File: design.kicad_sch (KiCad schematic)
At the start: 11 parts, among them J1 Conn_01x03_Female

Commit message: scramble
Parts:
- J1: footprint Connector_PinHeader_2.54mm:PinHeader_1x03_P2.54mm_Horizontal -> Connector_PinHeader_2.54mm:PinHeader_1x03_P2.54mm_Vertical
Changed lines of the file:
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@@
     (property "Reference" "J1" (id 0) (at 70.485 77.47 0))
     (property "Value" "Conn_01x03_Female" (id 1) (at 70.485 80.01 0))
-    (property "Footprint" "Connector_PinHeader_2.54mm:PinHeader_1x03_P2.54mm_Horizontal" (id 2) (at 69.85 85.09 0)
+    (property "Footprint" "Connector_PinHeader_2.54mm:PinHeader_1x03_P2.54mm_Vertical" (id 2) (at 69.85 85.09 0)
       (effects (font (size 1.27 1.27)) hide)
     )
@@
     )
     (path "/59340309-930f-44a7-9dc0-119af0640901"
-      (reference "J1") (unit 1) (value "Conn_01x03_Female") (footprint "Connector_PinHeader_2.54mm:PinHeader_1x03_P2.54mm_Horizontal")
+      (reference "J1") (unit 1) (value "Conn_01x03_Female") (footprint "Connector_PinHeader_2.54mm:PinHeader_1x03_P2.54mm_Vertical")
     )
     (path "/befcbf5f-cf66-4a10-8c7a-e7785ca8eeda"

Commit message: changed to custom sk6805 footprint
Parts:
- D1, D2, D3, D4, D5, D6, D7, D8, D9: footprint LED_SMD:LED_SK6812_EC15_1.5x1.5mm -> LED_custom:LED_SK6805_EC15_1.5x1.5mm
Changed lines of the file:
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@@
     (property "Reference" "D4" (id 0) (at 115.57 114.4143 0))
     (property "Value" "SK6805_1515" (id 1) (at 115.57 116.9543 0))
-    (property "Footprint" "LED_SMD:LED_SK6812_EC15_1.5x1.5mm" (id 2) (at 104.14 126.365 0)
+    (property "Footprint" "LED_custom:LED_SK6805_EC15_1.5x1.5mm" (id 2) (at 104.14 126.365 0)
       (effects (font (size 1.27 1.27)) (justify left top) hide)
     )
@@
     (property "Reference" "D2" (id 0) (at 149.225 80.7593 0))
     (property "Value" "SK6805_1515" (id 1) (at 149.225 83.2993 0))
-    (property "Footprint" "LED_SMD:LED_SK6812_EC15_1.5x1.5mm" (id 2) (at 137.795 92.71 0)
+    (property "Footprint" "LED_custom:LED_SK6805_EC15_1.5x1.5mm" (id 2) (at 137.795 92.71 0)
       (effects (font (size 1.27 1.27)) (justify left top) hide)
     )
@@
     (property "Reference" "D8" (id 0) (at 149.225 146.1643 0))
     (property "Value" "SK6805_1515" (id 1) (at 149.225 148.7043 0))
-    (property "Footprint" "LED_SMD:LED_SK6812_EC15_1.5x1.5mm" (id 2) (at 137.795 158.115 0)
+    (property "Footprint" "LED_custom:LED_SK6805_EC15_1.5x1.5mm" (id 2) (at 137.795 158.115 0)
       (effects (font (size 1.27 1.27)) (justify left top) hide)
     )
@@
     (property "Reference" "D6" (id 0) (at 181.61 114.4143 0))
     (property "Value" "SK6805_1515" (id 1) (at 181.61 116.9543 0))
-    (property "Footprint" "LED_SMD:LED_SK6812_EC15_1.5x1.5mm" (id 2) (at 170.18 126.365 0)
+    (property "Footprint" "LED_custom:LED_SK6805_EC15_1.5x1.5mm" (id 2) (at 170.18 126.365 0)
       (effects (font (size 1.27 1.27)) (justify left top) hide)
     )
@@
     (property "Reference" "D3" (id 0) (at 181.61 80.7593 0))
     (property "Value" "SK6805_1515" (id 1) (at 181.61 83.2993 0))
-    (property "Footprint" "LED_SMD:LED_SK6812_EC15_1.5x1.5mm" (id 2) (at 170.18 92.71 0)
+    (property "Footprint" "LED_custom:LED_SK6805_EC15_1.5x1.5mm" (id 2) (at 170.18 92.71 0)
       (effects (font (size 1.27 1.27)) (justify left top) hide)
     )
@@
     (property "Reference" "D7" (id 0) (at 115.57 146.1643 0))
     (property "Value" "SK6805_1515" (id 1) (at 115.57 148.7043 0))
-    (property "Footprint" "LED_SMD:LED_SK6812_EC15_1.5x1.5mm" (id 2) (at 104.14 158.115 0)
+    (property "Footprint" "LED_custom:LED_SK6805_EC15_1.5x1.5mm" (id 2) (at 104.14 158.115 0)
       (effects (font (size 1.27 1.27)) (justify left top) hide)
     )
@@
     (property "Reference" "D1" (id 0) (at 115.57 80.7593 0))
     (property "Value" "SK6805_1515" (id 1) (at 115.57 83.2993 0))
-    (property "Footprint" "LED_SMD:LED_SK6812_EC15_1.5x1.5mm" (id 2) (at 104.14 92.71 0)
+    (property "Footprint" "LED_custom:LED_SK6805_EC15_1.5x1.5mm" (id 2) (at 104.14 92.71 0)
       (effects (font (size 1.27 1.27)) (justify left top) hide)
     )
@@
     (property "Reference" "D5" (id 0) (at 149.225 114.4143 0))
     (property "Value" "SK6805_1515" (id 1) (at 149.225 116.9543 0))
-    (property "Footprint" "LED_SMD:LED_SK6812_EC15_1.5x1.5mm" (id 2) (at 137.795 126.365 0)
+    (property "Footprint" "LED_custom:LED_SK6805_EC15_1.5x1.5mm" (id 2) (at 137.795 126.365 0)
       (effects (font (size 1.27 1.27)) (justify left top) hide)
     )
@@
     (property "Reference" "D9" (id 0) (at 181.61 146.1643 0))
     (property "Value" "SK6805_1515" (id 1) (at 181.61 148.7043 0))
-    (property "Footprint" "LED_SMD:LED_SK6812_EC15_1.5x1.5mm" (id 2) (at 170.18 158.115 0)
+    (property "Footprint" "LED_custom:LED_SK6805_EC15_1.5x1.5mm" (id 2) (at 170.18 158.115 0)
       (effects (font (size 1.27 1.27)) (justify left top) hide)
     )
@@
     )
     (path "/e522fa02-5074-425d-83fb-e4bbcbcfc1cc"
-      (reference "D1") (unit 1) (value "SK6805_1515") (footprint "LED_SMD:LED_SK6812_EC15_1.5x1.5mm")
+      (reference "D1") (unit 1) (value "SK6805_1515") (footprint "LED_custom:LED_SK6805_EC15_1.5x1.5mm")
     )
     (path "/326bef75-2474-4757-9969-0d52eb3a4e5b"
-      (reference "D2") (unit 1) (value "SK6805_1515") (footprint "LED_SMD:LED_SK6812_EC15_1.5x1.5mm")
+      (reference "D2") (unit 1) (value "SK6805_1515") (footprint "LED_custom:LED_SK6805_EC15_1.5x1.5mm")
     )
     (path "/c46ac134-249e-4d65-803c-35a49384ddd5"
-      (reference "D3") (unit 1) (value "SK6805_1515") (footprint "LED_SMD:LED_SK6812_EC15_1.5x1.5mm")
+      (reference "D3") (unit 1) (value "SK6805_1515") (footprint "LED_custom:LED_SK6805_EC15_1.5x1.5mm")
     )
     (path "/0f6926e5-6644-4b79-84dc-a15428edfea6"
-      (reference "D4") (unit 1) (value "SK6805_1515") (footprint "LED_SMD:LED_SK6812_EC15_1.5x1.5mm")
+      (reference "D4") (unit 1) (value "SK6805_1515") (footprint "LED_custom:LED_SK6805_EC15_1.5x1.5mm")
     )
     (path "/e740ed92-176d-41c6-a6ef-8356517a9b21"
-      (reference "D5") (unit 1) (value "SK6805_1515") (footprint "LED_SMD:LED_SK6812_EC15_1.5x1.5mm")
+      (reference "D5") (unit 1) (value "SK6805_1515") (footprint "LED_custom:LED_SK6805_EC15_1.5x1.5mm")
     )
     (path "/9e8445ed-d095-47a8-9fdd-69266b92c7fc"
-      (reference "D6") (unit 1) (value "SK6805_1515") (footprint "LED_SMD:LED_SK6812_EC15_1.5x1.5mm")
+      (reference "D6") (unit 1) (value "SK6805_1515") (footprint "LED_custom:LED_SK6805_EC15_1.5x1.5mm")
     )
     (path "/e3cc88c2-3cef-4b90-bc40-cc4c2adb5e11"
-      (reference "D7") (unit 1) (value "SK6805_1515") (footprint "LED_SMD:LED_SK6812_EC15_1.5x1.5mm")
+      (reference "D7") (unit 1) (value "SK6805_1515") (footprint "LED_custom:LED_SK6805_EC15_1.5x1.5mm")
     )
     (path "/3d2278a1-321e-4788-9220-d685cf2da13b"
-      (reference "D8") (unit 1) (value "SK6805_1515") (footprint "LED_SMD:LED_SK6812_EC15_1.5x1.5mm")
+      (reference "D8") (unit 1) (value "SK6805_1515") (footprint "LED_custom:LED_SK6805_EC15_1.5x1.5mm")
     )
     (path "/e75bc03a-4679-4570-90ad-d871a1d0bbc5"
-      (reference "D9") (unit 1) (value "SK6805_1515") (footprint "LED_SMD:LED_SK6812_EC15_1.5x1.5mm")
+      (reference "D9") (unit 1) (value "SK6805_1515") (footprint "LED_custom:LED_SK6805_EC15_1.5x1.5mm")
     )
     (path "/59340309-930f-44a7-9dc0-119af0640901"

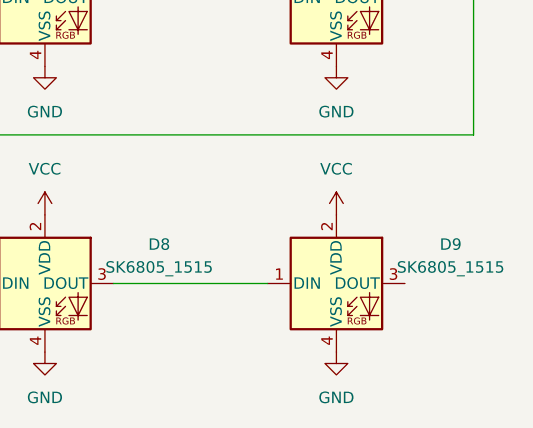
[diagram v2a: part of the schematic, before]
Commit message: error from ERC
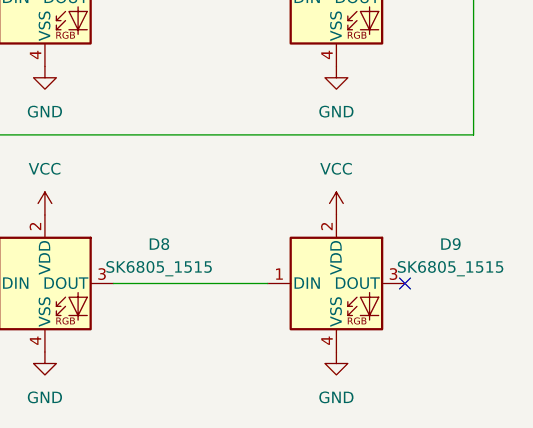
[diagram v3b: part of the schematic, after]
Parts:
- D1, D2, D3, D4, D5, D6, D7, D8, D9: footprint LED_custom:LED_SK6805_EC15_1.5x1.5mm -> LED_SMD:LED_SK6812_EC15_1.5x1.5mm
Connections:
- no-connect marks 0 -> 1
